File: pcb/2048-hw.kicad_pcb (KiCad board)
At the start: 2 copper layers, 60 x 93 mm, 97 parts, among them J1 UJC-HP-3-SMT-TR, J2 Battery, J3 SWD, SW1 SW_SPDT, SW2 PUSH_A, SW3 PUSH_B, U1 STM32F303K8Tx, U2 MCP73831-2-OT, U3 AP2210N-3.3TRG1, U4 PSP_1000_JSTK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

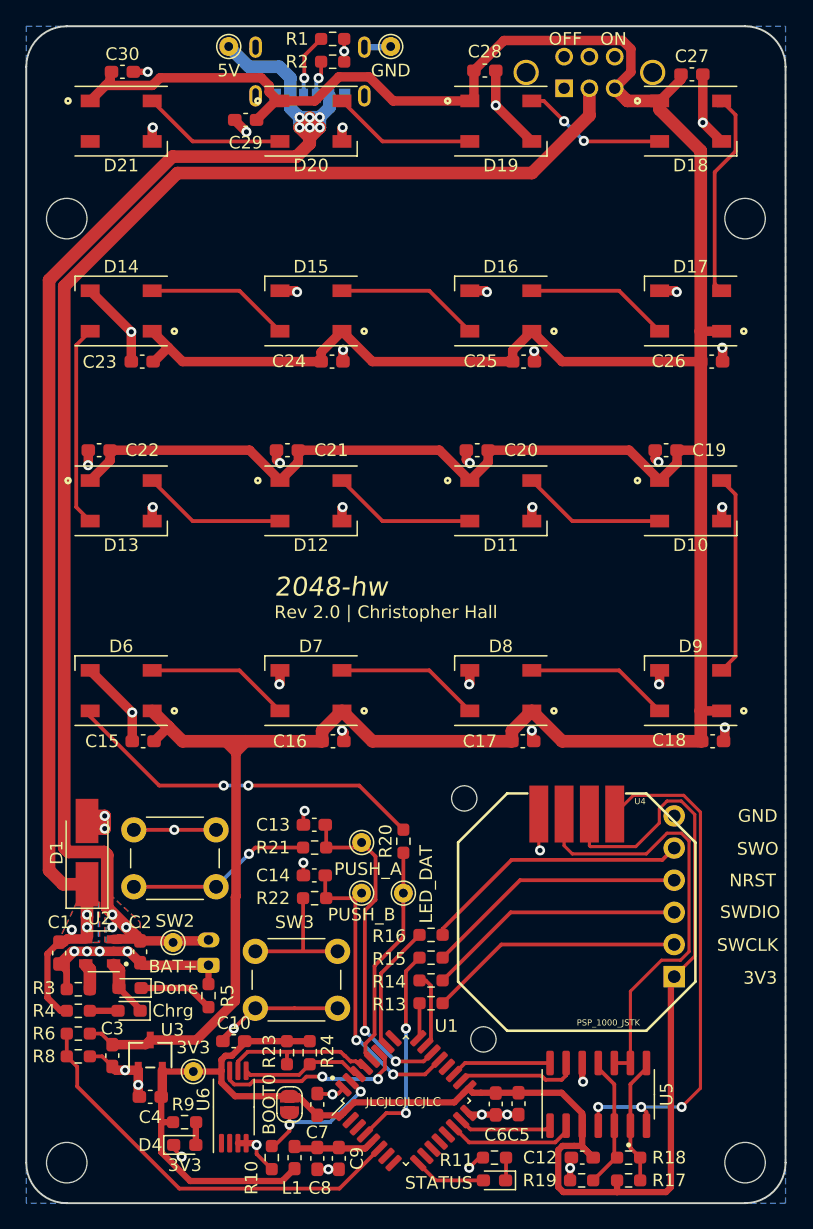
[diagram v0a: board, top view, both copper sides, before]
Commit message: pcb: Charge battery/power stuff independent of one another
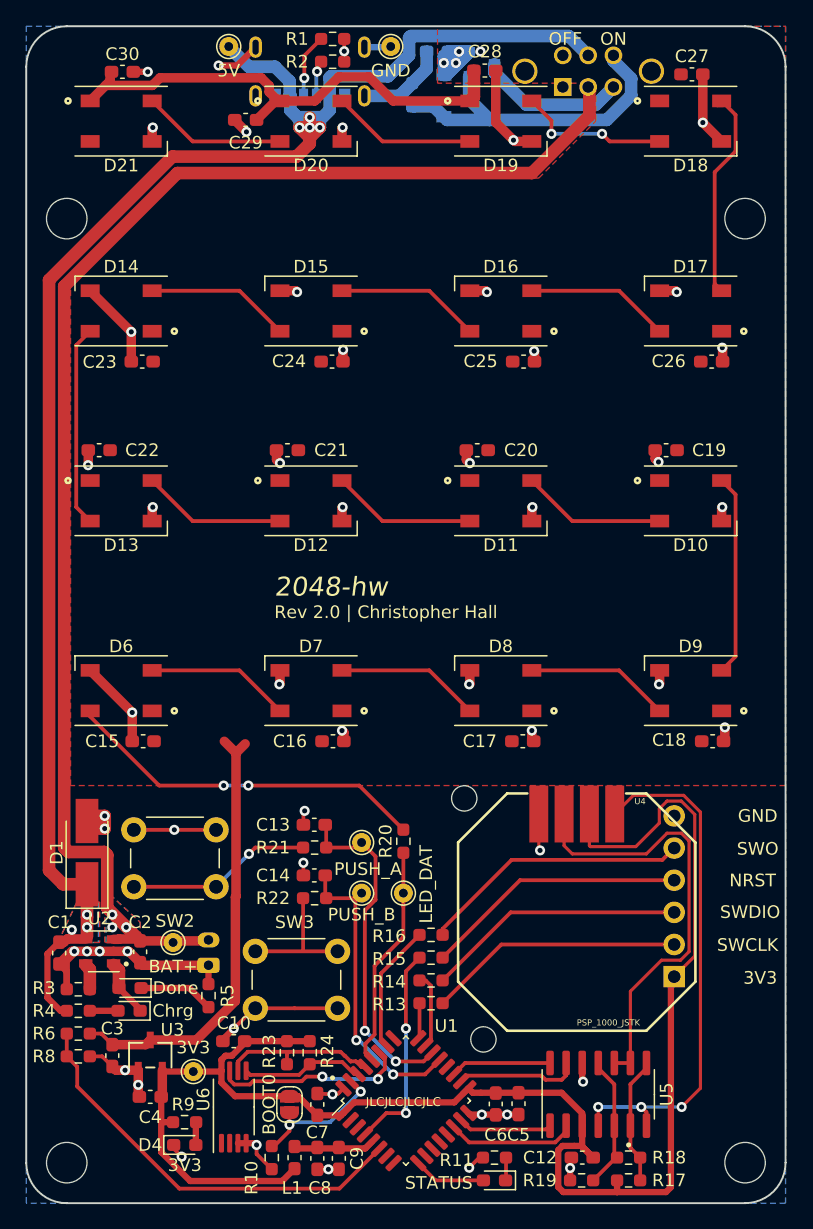
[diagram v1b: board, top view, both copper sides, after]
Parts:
- added C11: 1u, Capacitor_SMD:C_0603_1608Metric_Pad1.08x0.95mm_HandSolder, B.Cu at (152.5, 62.0)
- added D22: ds30308, Diode_SMD:D_SOD-123, B.Cu at (153.0, 65.5)
- added Q1: PMV27UPE, Package_TO_SOT_SMD:SOT-23, B.Cu at (156.0, 63.0)
- added R7: 100k, Resistor_SMD:R_0603_1608Metric_Pad0.98x0.95mm_HandSolder, B.Cu at (150.5, 65.4)
- SW1: value SW_SPDT -> SW_DPDT_x2
- moved SW1 0.14 mm to (162.4, 64.8)
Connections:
- SW1 pad 3: V_BAT -> Net-(Q1-Pad3)
- SW1 pad 4: (no net) -> Net-(SW1-Pad4)
- SW1 pad 5: (no net) -> +5V
- SW1 pad 6: (no net) -> Net-(D22-Pad2)
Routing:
- net V_BAT: track 313.6 -> 82.6 mm, vias 0 -> 4
- net Net-(D22-Pad2): track 0.00 -> 26.4 mm
- net +5V: track 117.1 -> 141.4 mm, vias 9 -> 7
- net Net-(Q1-Pad3): track 0.00 -> 11.7 mm
- net GND: track 128.9 -> 140.3 mm, vias 51 -> 52
- net Net-(D18-Pad2): track 11.4 -> 12.0 mm
- added copper zone on F.Cu, net V_BAT

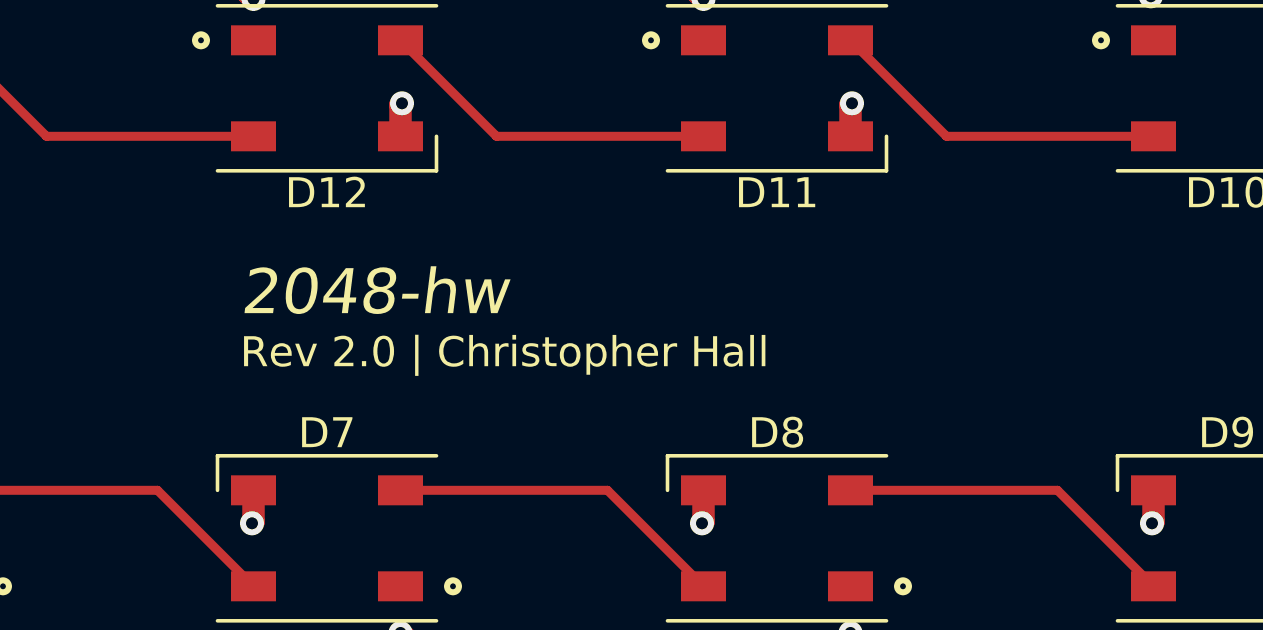
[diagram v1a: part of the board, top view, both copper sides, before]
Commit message: pcb: Tidy up routing
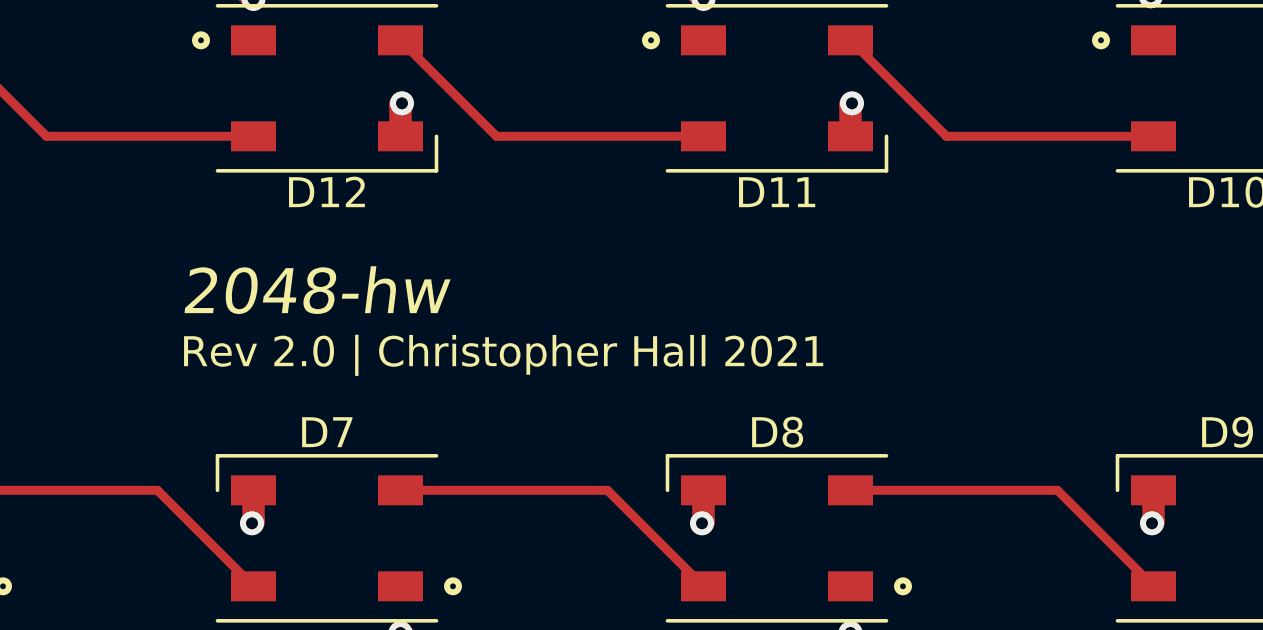
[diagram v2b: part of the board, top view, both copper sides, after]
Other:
- board text added: "Rev 2.0 | Christopher Hall 2021"
- board text removed: "Rev 2.0 | Christopher Hall"
